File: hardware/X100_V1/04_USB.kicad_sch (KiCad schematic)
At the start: 16 parts, among them J401 USB4105-GF-A, U401 TPD2E2U06QDBZRQ1, U402 SN74LVC1G17DBVR, U403 TPD2E2U06QDBZRQ1, U404 TPD2E2U06QDBZRQ1

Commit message: Refactor X100 schematics for readability
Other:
- note added: "04 USB通信与保护 / USB INTERFACE AND PROTECTION"
- note added: "CC 配置与保护 / CC CONFIGURATION AND ESD"
- note added: "USB DP / DM"
- note added: "USB Type-C 接口 / USB TYPE-C CONNECTOR"
- note added: "USB 数据线 ESD / DP-DM ESD"
- note added: "VBUS / POWER / GND"
- note added: "VBUS 保护 / USB VBUS PROTECTION"
- note added: "VBUS 检测 / VBUS SENSE"
- moved on the sheet: C401, C402, J401, R401, R402, R403, R404, TP401, TP402, TP403, TP404, TP405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

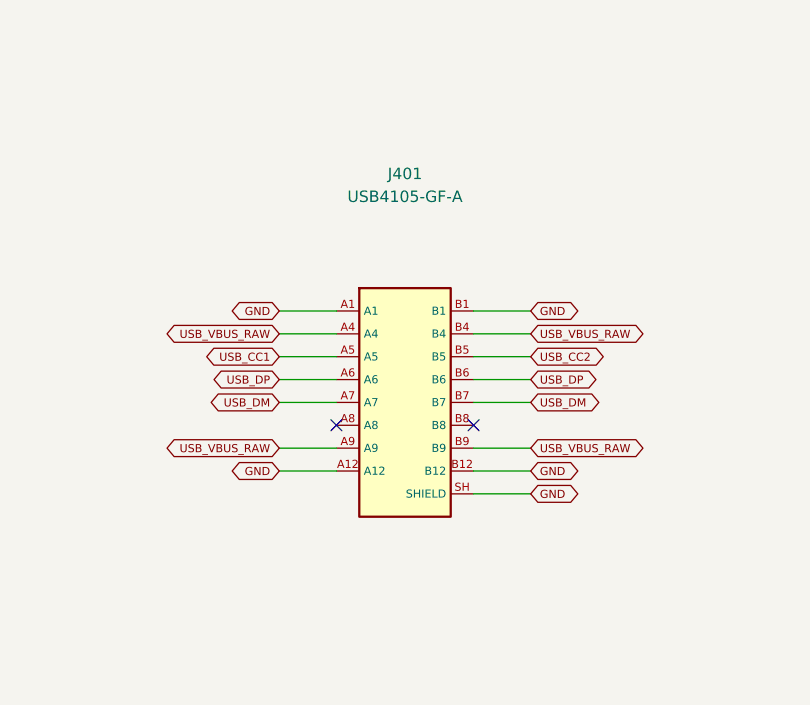
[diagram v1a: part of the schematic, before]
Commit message: fix(pcb): apply approved Amphenol J401 with native netlist sync
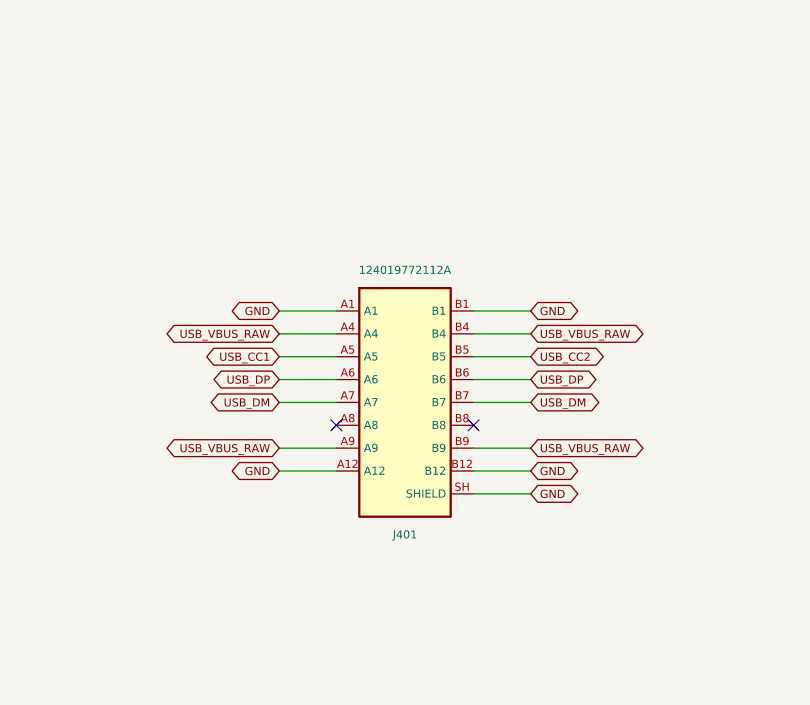
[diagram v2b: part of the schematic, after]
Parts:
- J401: value USB4105-GF-A -> 124019772112A; footprint X100_Physical:Official_Connector_USB_USB_C_Receptacle_GCT_USB4105-xx-A_16P_TopMnt_Horizontal -> X100_Physical:Official_USB_C_Amphenol_124019772112A; symbol X100_Physical:GCT_USB4105_GF_A -> X100_Physical:Amphenol_124019772112A; LCSC (none) -> C5430474; MPN USB4105-GF-A -> 124019772112A; Manufacturer GCT -> Amphenol; Mechanical Assembly (none) -> Top mount; PCB 1.6mm; 0.50mm SH projection embedded in plat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; Package default0.95mm stake Type-C16P -> USB-C dual-row SMT / 4 plated SH slots; Procurement Approval (none) -> USER_APPROVED_2026-10-22; Selection Status (none) -> FINAL_SELECTED_FOR_V1; Verification Status (none) -> DESIGN_REVIEWED_BENCH_PENDING
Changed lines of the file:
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@@
 	)
 	(symbol
-		(lib_id "X100_Physical:GCT_USB4105_GF_A")
+		(lib_id "X100_Physical:Amphenol_124019772112A")
 		(at 119.38 114.3 0)
 		(unit 1)
+		(body_style 1)
 		(exclude_from_sim no)
 		(in_bom yes)
 		(on_board yes)
+		(in_pos_files yes)
 		(dnp no)
 		(property "Reference" "J401"
-			(at 119.38 88.9 0)
+			(at 119.38 129 0)
+			(show_name no)
+			(do_not_autoplace no)
+			(effects
+				(font
+					(size 0.9 0.9)
+				)
+			)
+		)
+		(property "Value" "124019772112A"
+			(at 119.38 99.6 0)
+			(show_name no)
+			(do_not_autoplace no)
+			(effects
+				(font
+					(size 0.9 0.9)
+				)
+			)
+		)
+		(property "Footprint" "X100_Physical:Official_USB_C_Amphenol_124019772112A"
+			(at 119.38 114.3 0)
+			(hide yes)
+			(show_name no)
+			(do_not_autoplace no)
+			(effects
+				(font
+					(size 0.9 0.9)
+				)
+			)
+		)
+		(property "Datasheet" "https://cdn.amphenol-cs.com/media/wysiwyg/files/drawing/c12401977-3.pdf"
+			(at 119.38 114.3 0)
+			(hide yes)
+			(show_name no)
+			(do_not_autoplace no)
+			(effects
+				(font
+					(size 0.9 0.9)
+				)
+			)
+		)
+		(property "Description" ""
+			(at 119.38 114.3 0)
+			(hide yes)
+			(show_name no)
+			(do_not_autoplace no)
 			(effects
 				(font
@@
 			)
 		)
-		(property "Value" "USB4105-GF-A"
-			(at 119.38 91.44 0)
+		(property "Manufacturer" "Amphenol"
+			(at 119.38 114.3 0)
 			(effects
 				(font
 					(size 1.27 1.27)
 				)
+				(hide yes)
 			)
 		)
-		(property "Footprint" "X100_Physical:Official_Connector_USB_USB_C_Receptacle_GCT_USB4105-xx-A_16P_TopMnt_Horizontal"
+		(property "MPN" "124019772112A"
 			(at 119.38 114.3 0)
 			(effects
 				(font
-					(size 0.9 0.9)
+					(size 1.27 1.27)
 				)
 				(hide yes)
 			)
 		)
-		(property "Datasheet" "https://www.gct.co/files/drawings/usb4105.pdf"
+		(property "Package" "USB-C dual-row SMT / 4 plated SH slots"
 			(at 119.38 114.3 0)
 			(effects
 				(font
-					(size 0.9 0.9)
-				)
-				(hide yes)
-			)
-		)
-		(property "Manufacturer" "GCT"
-			(at 119.38 114.3 0)
-			(effects
-				(font
-					(size 0.9 0.9)
-				)
-				(hide yes)
-			)
-		)
-		(property "MPN" "USB4105-GF-A"
-			(at 119.38 114.3 0)
-			(effects
-				(font
-					(size 0.9 0.9)
-				)
-				(hide yes)
-			)
-		)
-		(property "Package" "default0.95mm stake Type-C16P"
-			(at 119.38 114.3 0)
-			(effects
-				(font
-					(size 0.9 0.9)
+					(size 1.27 1.27)
 				)
 				(hide yes)
@@
 			(effects
 				(font
-					(size 0.9 0.9)
+					(size 1.27 1.27)
 				)
 				(hide yes)
 			)
 		)
-		(instances
-			(project "X100_CleanSheet"
-				(path "/8ca41881-cb11-48b5-8b6a-9e8c99402ac3/b5486f2c-43ef-4124-ae2d-8650a60747f3"
-					(reference "J401")
-					(unit 1)
+		(property "LCSC" "C5430474"
+			(at 119.38 114.3 0)
+			(effects
+				(font
+					(size 1.27 1.27)
 				)
+				(hide yes)
+			)
+		)
+		(property "Selection Status" "FINAL_SELECTED_FOR_V1"
+			(at 119.38 114.3 0)
+			(effects
+				(font
+					(size 1.27 1.27)
+				)
+				(hide yes)
+			)
+		)
+		(property "Verification Status" "DESIGN_REVIEWED_BENCH_PENDING"
+			(at 119.38 114.3 0)
+			(effects
+				(font
+					(size 1.27 1.27)
+				)
+				(hide yes)
+			)
+		)
+		(property "Procurement Approval" "USER_APPROVED_2026-10-22"
+			(at 119.38 114.3 0)
+			(effects
+				(font
+					(size 1.27 1.27)
+				)
+				(hide yes)
+			)
+		)
+		(property "Mechanical Assembly" "Top mount; PCB 1.6mm; 0.50mm SH projection embedded in plated slots; solder from component side; inspect joint wetting"
+			(at 119.38 114.3 0)
+			(effects
+				(font
+					(size 1.27 1.27)
+				)
+				(hide yes)
 			)
 		)
 		(pin "A1"
+		)
+		(pin "A12"
 		)
 		(pin "A4"
@@
 		(pin "A9"
 		)
-		(pin "A12"
+		(pin "B1"
 		)
-		(pin "B1"
+		(pin "B12"
 		)
 		(pin "B4"
@@
 		(pin "B9"
 		)
-		(pin "B12"
-		)
 		(pin "SH"
 		)
+		(instances
+			(project "X100_CleanSheet"
+				(path "/8ca41881-cb11-48b5-8b6a-9e8c99402ac3/b5486f2c-43ef-4124-ae2d-8650a60747f3"
+					(reference "J401")
+					(unit 1)
+				)
+			)
+		)
 	)

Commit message: 紧凑测试点保留65处可测性并消除46对courtyard重叠
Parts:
- TP401, TP402, TP405: footprint X100_Physical:TP1p5_NoPaste -> X100_Physical:TP0p6_Inline_NoPaste; Layout Note (none) -> 0.6mm probe land, unchanged 0.5mm probe envelope; fine-tip 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; MPN TP1p5 -> PCB_TESTPAD_0P6_NO_PASTE; Package 1.5mm top probe -> PCB feature: 0.6mm exposed round test land; no paste
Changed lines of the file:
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@@
 			)
 		)
-		(property "Footprint" "X100_Physical:TP1p5_NoPaste"
+		(property "Footprint" "X100_Physical:TP0p6_Inline_NoPaste"
 			(at 284.48 342.9 0)
 			(effects
@@
 			)
 		)
-		(property "MPN" "TP1p5"
+		(property "MPN" "PCB_TESTPAD_0P6_NO_PASTE"
 			(at 284.48 342.9 0)
 			(effects
@@
 			)
 		)
-		(property "Package" "1.5mm top probe"
+		(property "Package" "PCB feature: 0.6mm exposed round test land; no paste"
 			(at 284.48 342.9 0)
 			(effects
@@
 			)
 		)
+    (property "Layout Note" "0.6mm probe land, unchanged 0.5mm probe envelope; fine-tip probing; all 65 net accesses retained" (at 284.48 342.9 0)
+      (effects (font (size 1.27 1.27)) (hide yes))
+    )
 		(instances
 			(project "X100_CleanSheet"
@@
 			)
 		)
-		(property "Footprint" "X100_Physical:TP1p5_NoPaste"
+		(property "Footprint" "X100_Physical:TP0p6_Inline_NoPaste"
 			(at 375.92 342.9 0)
 			(effects
@@
 			)
 		)
-		(property "MPN" "TP1p5"
+		(property "MPN" "PCB_TESTPAD_0P6_NO_PASTE"
 			(at 375.92 342.9 0)
 			(effects
@@
 			)
 		)
-		(property "Package" "1.5mm top probe"
+		(property "Package" "PCB feature: 0.6mm exposed round test land; no paste"
 			(at 375.92 342.9 0)
 			(effects
@@
 			)
 		)
+    (property "Layout Note" "0.6mm probe land, unchanged 0.5mm probe envelope; fine-tip probing; all 65 net accesses retained" (at 375.92 342.9 0)
+      (effects (font (size 1.27 1.27)) (hide yes))
+    )
 		(instances
 			(project "X100_CleanSheet"
@@
 			)
 		)
-		(property "Footprint" "X100_Physical:TP1p5_NoPaste"
+		(property "Footprint" "X100_Physical:TP0p6_Inline_NoPaste"
 			(at 375.92 363.22 0)
 			(effects
@@
 			)
 		)
-		(property "MPN" "TP1p5"
+		(property "MPN" "PCB_TESTPAD_0P6_NO_PASTE"
 			(at 375.92 363.22 0)
 			(effects
@@
 			)
 		)
-		(property "Package" "1.5mm top probe"
+		(property "Package" "PCB feature: 0.6mm exposed round test land; no paste"
 			(at 375.92 363.22 0)
 			(effects
@@
 			)
 		)
+    (property "Layout Note" "0.6mm probe land, unchanged 0.5mm probe envelope; fine-tip probing; all 65 net accesses retained" (at 375.92 363.22 0)
+      (effects (font (size 1.27 1.27)) (hide yes))
+    )
 		(instances
 			(project "X100_CleanSheet"
